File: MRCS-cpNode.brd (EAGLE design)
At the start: 99.8 x 68.8 mm, 46 parts, among them P1 CA CC, U1 MAX3465CPD, U2 NE555P

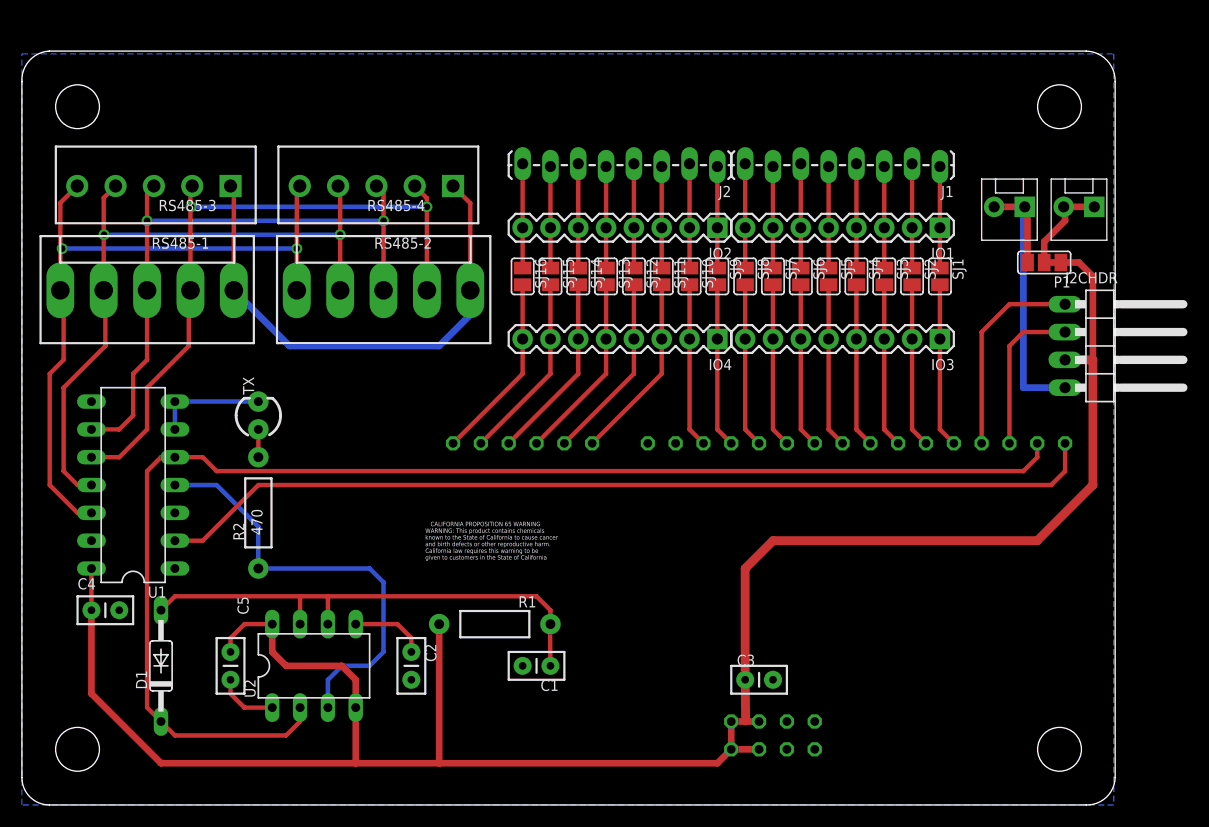
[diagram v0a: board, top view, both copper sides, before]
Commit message: added 6-pin headers, fixed DCR errors
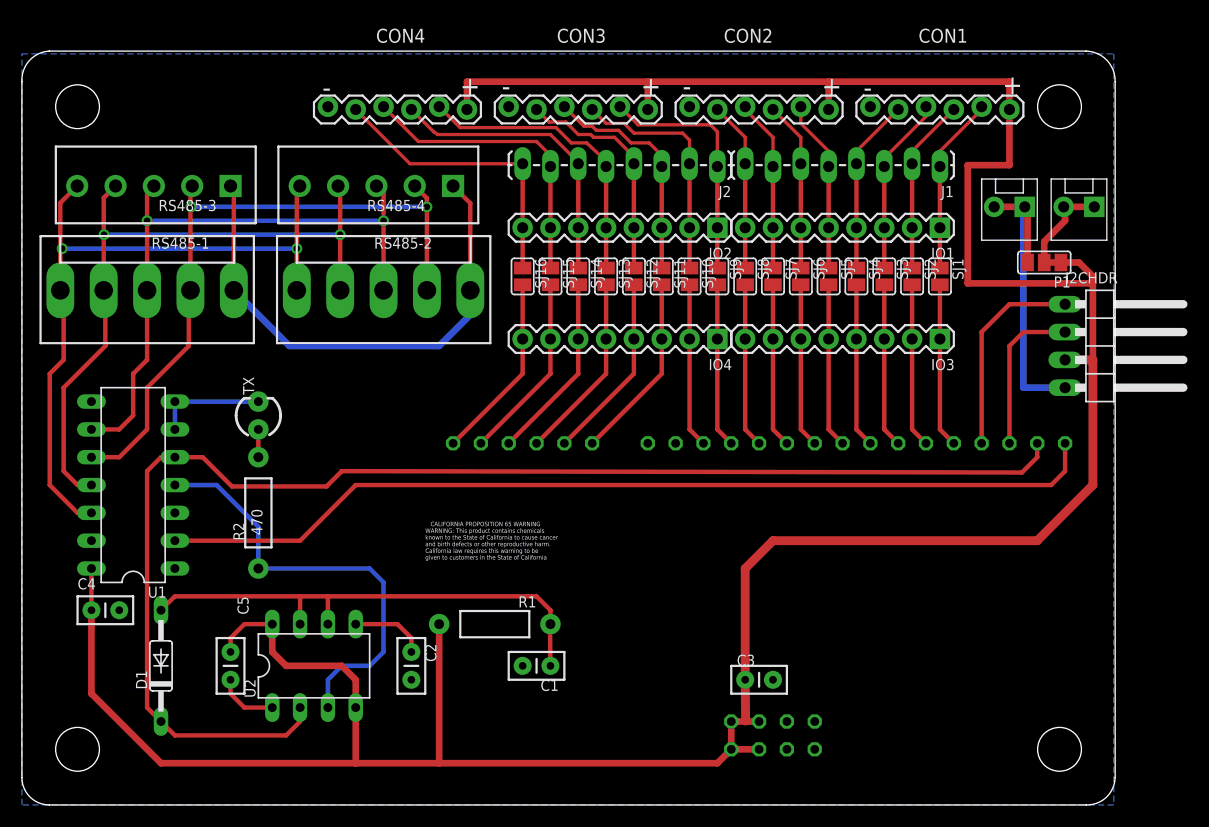
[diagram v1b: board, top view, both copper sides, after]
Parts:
- added CON1, CON2, CON3, CON4: (no value), SPCoast:1X06-SIP_LOCK
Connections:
- removed net N$1: IO1.2, J1.2, SJ2.1
- removed net N$10: IO2.2, J2.2, SJ10.1
- removed net N$2: IO1.1, J1.1, SJ1.1
- removed net N$21: IO2.4, J2.4, SJ12.1
- removed net N$3: IO1.3, J1.3, SJ3.1
- removed net N$30: IO2.5, J2.5, SJ13.1
- removed net N$31: IO2.6, J2.6, SJ14.1
- removed net N$32: IO2.7, J2.7, SJ15.1
- removed net N$33: IO2.8, J2.8, SJ16.1
- removed net N$4: IO1.4, J1.4, SJ4.1
- removed net N$43: IO2.3, J2.3, SJ11.1
- removed net N$5: IO1.5, J1.5, SJ5.1
- removed net N$6: IO1.6, J1.6, SJ6.1
- removed net N$7: IO1.7, J1.7, SJ7.1
- removed net N$8: IO1.8, J1.8, SJ8.1
- removed net N$9: IO2.1, J2.1, SJ9.1
- new net O1: CON1.2, IO1.1, J1.1, SJ1.1
- new net O10: CON3.3, IO2.2, J2.2, SJ10.1
- new net O11: CON3.4, IO2.3, J2.3, SJ11.1
- new net O12: CON3.5, IO2.4, J2.4, SJ12.1
- new net O13: CON4.2, IO2.5, J2.5, SJ13.1
- new net O14: CON4.3, IO2.6, J2.6, SJ14.1
- new net O15: CON4.4, IO2.7, J2.7, SJ15.1
- new net O16: CON4.5, IO2.8, J2.8, SJ16.1
- new net O2: CON1.3, IO1.2, J1.2, SJ2.1
- new net O3: CON1.4, IO1.3, J1.3, SJ3.1
- new net O4: CON1.5, IO1.4, J1.4, SJ4.1
- new net O5: CON2.2, IO1.5, J1.5, SJ5.1
- new net O6: CON2.3, IO1.6, J1.6, SJ6.1
- new net O7: CON2.4, IO1.7, J1.7, SJ7.1
- new net O8: CON2.5, IO1.8, J1.8, SJ8.1
- new net O9: CON3.2, IO2.1, J2.1, SJ9.1
- net GND: now also CON1.6, CON2.6, CON3.6, CON4.6
- net VCC: now also CON1.1, CON2.1, CON3.1, CON4.1
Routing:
- net VCC: track 191.7 -> 282.5 mm
- net O15: track 0.00 -> 27.4 mm
- net O14: track 0.00 -> 27.3 mm
- net O13: track 0.00 -> 27.0 mm
- net O16: track 0.00 -> 26.8 mm
- net O9: track 0.00 -> 22.3 mm
- net O10: track 0.00 -> 21.7 mm
- net O11: track 0.00 -> 21.0 mm
- net O12: track 0.00 -> 20.8 mm
- net O3: track 0.00 -> 16.3 mm
- net O1: track 0.00 -> 16.3 mm
- net O4: track 0.00 -> 16.1 mm
- net O2: track 0.00 -> 16.1 mm
- net O7: track 0.00 -> 15.8 mm
- net O5: track 0.00 -> 15.8 mm
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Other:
- board text added: "+"
- board text added: "-"
- board text added: "2020-01"
- board text added: "v2.6"
- board text removed: "2019-07"
- board text removed: "v2.5Cp"

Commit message: added missing values
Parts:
- BBLEO: value (none) -> Footprint
- CON1, CON2, CON3, CON4, GND, IO1, IO2, IO3, IO4, J1, J2, LEDCOM: value (none) -> 0.100
- R1: value (none) -> 12k
- SJ1, SJ10, SJ11, SJ12, SJ13, SJ14, SJ15, SJ16, SJ2, SJ3, SJ4, SJ5, SJ6, SJ7, SJ8, SJ9: value (none) -> OFF
- TX: value (none) -> G
- U$2: value CA-PROP65WARNING -> Prop65
- U$3: value (none) -> MRCS

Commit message: added missing values
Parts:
- I2CHDR: value (none) -> 0.100
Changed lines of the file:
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@@
 </element>
 <element name="GND" library="SparkFun" package="MOLEX-1X2_LOCK" value="0.100" x="91.44" y="54.61" smashed="yes" rot="R180"/>
-<element name="I2CHDR" library="pinhead" package="1X04/90" value="" x="99.06" y="41.91" smashed="yes" rot="R270">
+<element name="I2CHDR" library="pinhead" package="1X04/90" value="0.100" x="99.06" y="41.91" smashed="yes" rot="R270">
 <attribute name="NAME" x="95.25" y="47.625" size="1.016" layer="25" font="vector" ratio="10"/>
 <attribute name="VALUE" x="94.615" y="34.925" size="1.27" layer="27"/>

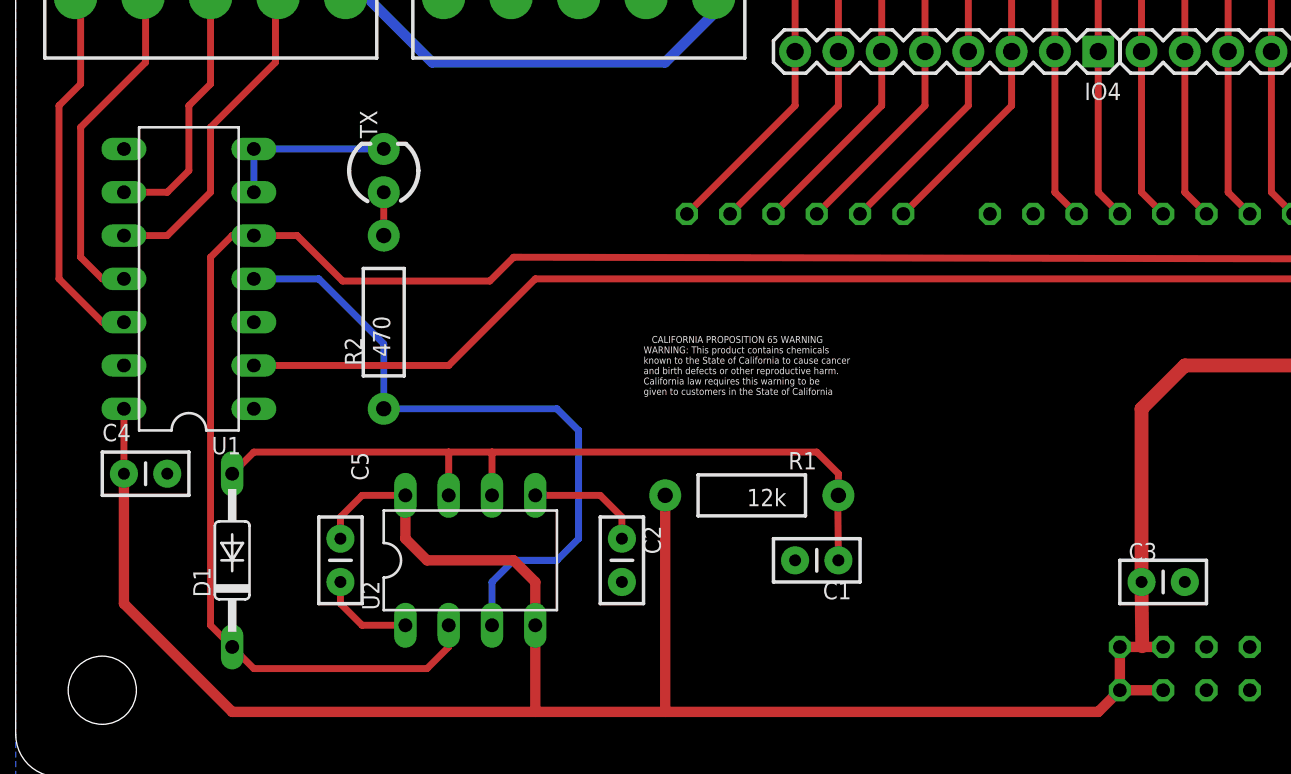
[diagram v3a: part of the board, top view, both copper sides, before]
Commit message: normalized values
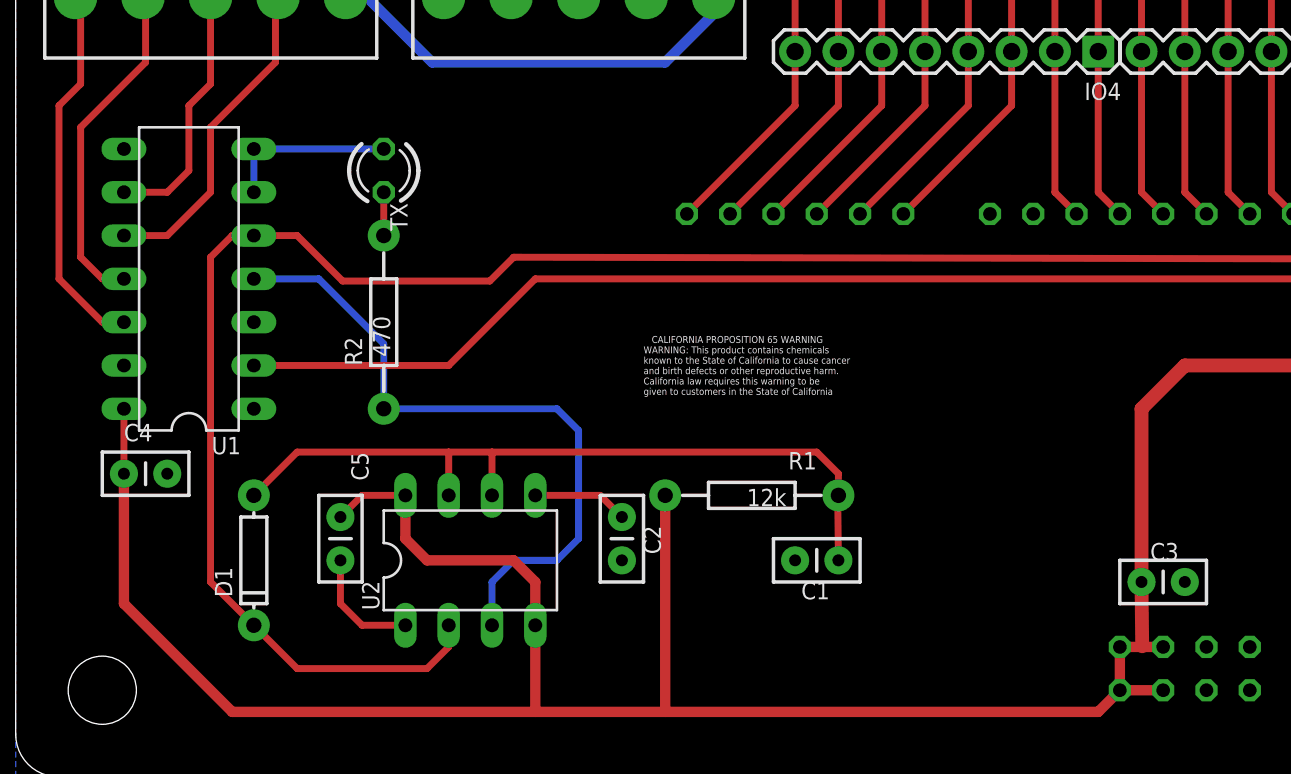
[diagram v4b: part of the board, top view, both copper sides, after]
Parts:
- BOARD1: value BOARD69X100MRCS -> BOARD
- C1: device SparkFun:CAP-PTH-SMALL2 -> SPCoast:C-PTH-0.100
- C2, C3, C4, C5: value .01uF -> 0.01uF; device SparkFun:CAP-PTH-SMALL2 -> SPCoast:C-PTH-0.100
- D1: value 1N4148DO35-10 -> 1N4148; device diode:DO35-10 -> SPCoast:DIODE-1N4148
- R1, R2: device SparkFun:AXIAL-0.4 -> SPCoast:AXIAL-0.4-RES
- RS485-1, RS485-2: value Molex -> 0.156
- TX: device SparkFun-LED:LED3MM -> SPCoast:LED3MM
- moved D1 1.27 mm to (14.0, 12.7)
- moved C4 1.27 mm to (7.62, 17.8)
- moved C1 1.27 mm to (47.0, 12.7)
- moved C3 1.27 mm to (67.3, 11.4)
- turned TX to 270 degrees
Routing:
- net TX: track 123.7 -> 122.3 mm
- net GND: track 44.2 -> 45.4 mm
- net N$38: track 6.88 -> 5.61 mm
- net VCC: track 282.5 -> 281.2 mm
- net N$52: track 46.8 -> 46.0 mm
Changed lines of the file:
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@@
 <elements>
 <element name="BBLEO" library="SPCoast" package="ARDUINO-BBLEO" value="Footprint" x="26.67" y="2.54" smashed="yes"/>
-<element name="BOARD1" library="SPCoast" package="BOARD-DINRAIL-2.71IN-MRCS" value="BOARD69X100MRCS" x="0" y="0" smashed="yes"/>
-<element name="C1" library="SparkFun" package="CAP-PTH-SMALL2" value="0.1uF" x="48.26" y="12.7" smashed="yes" rot="R180">
-<attribute name="NAME" x="49.022" y="11.43" size="1.016" layer="25" font="vector" ratio="10" rot="R180"/>
-<attribute name="VALUE" x="49.911" y="14.859" size="1.016" layer="27" font="vector" ratio="10" rot="R180"/>
-</element>
-<element name="C2" library="SparkFun" package="CAP-PTH-SMALL2" value=".01uF" x="35.56" y="13.97" smashed="yes" rot="R270">
+<element name="BOARD1" library="SPCoast" package="BOARD-DINRAIL-2.71IN-MRCS" value="BOARD" x="0" y="0" smashed="yes"/>
+<element name="C1" library="SPCoast" package="C-PTH-0.100" value="0.1uF" x="46.99" y="12.7" smashed="yes" rot="R180">
+<attribute name="NAME" x="47.752" y="11.43" size="1.016" layer="25" font="vector" ratio="10" rot="R180"/>
+<attribute name="VALUE" x="48.641" y="14.859" size="1.016" layer="27" font="vector" ratio="10" rot="R180"/>
+</element>
+<element name="C2" library="SPCoast" package="C-PTH-0.100" value="0.01uF" x="35.56" y="13.97" smashed="yes" rot="R270">
 <attribute name="NAME" x="36.83" y="14.732" size="1.016" layer="25" font="vector" ratio="10" rot="R270"/>
 <attribute name="VALUE" x="33.401" y="16.256" size="1.016" layer="27" font="vector" ratio="10" rot="R270"/>
 </element>
-<element name="C3" library="SparkFun" package="CAP-PTH-SMALL2" value=".01uF" x="66.04" y="11.43" smashed="yes">
-<attribute name="NAME" x="65.278" y="12.7" size="1.016" layer="25" font="vector" ratio="10"/>
-<attribute name="VALUE" x="64.389" y="9.271" size="1.016" layer="27" font="vector" ratio="10"/>
-</element>
-<element name="C4" library="SparkFun" package="CAP-PTH-SMALL2" value=".01uF" x="6.35" y="17.78" smashed="yes">
-<attribute name="NAME" x="5.08" y="19.685" size="1.016" layer="25" font="vector" ratio="10"/>
-<attribute name="VALUE" x="5.08" y="15.24" size="1.016" layer="27" font="vector" ratio="10"/>
-</element>
-<element name="C5" library="SparkFun" package="CAP-PTH-SMALL2" value=".01uF" x="19.05" y="13.97" smashed="yes" rot="R270">
+<element name="C3" library="SPCoast" package="C-PTH-0.100" value="0.01uF" x="67.31" y="11.43" smashed="yes">
+<attribute name="NAME" x="66.548" y="12.7" size="1.016" layer="25" font="vector" ratio="10"/>
+<attribute name="VALUE" x="65.659" y="9.271" size="1.016" layer="27" font="vector" ratio="10"/>
+</element>
+<element name="C4" library="SPCoast" package="C-PTH-0.100" value="0.01uF" x="7.62" y="17.78" smashed="yes">
+<attribute name="NAME" x="6.35" y="19.685" size="1.016" layer="25" font="vector" ratio="10"/>
+<attribute name="VALUE" x="6.35" y="15.24" size="1.016" layer="27" font="vector" ratio="10"/>
+</element>
+<element name="C5" library="SPCoast" package="C-PTH-0.100" value="0.01uF" x="19.05" y="13.97" smashed="yes" rot="R270">
 <attribute name="NAME" x="19.685" y="19.05" size="1.016" layer="25" font="vector" ratio="10" rot="R270"/>
 <attribute name="VALUE" x="17.78" y="20.32" size="1.016" layer="27" font="vector" ratio="10" rot="R270"/>
@@
 <attribute name="VALUE" x="40.64" y="59.055" size="1.016" layer="27" font="vector" ratio="10" rot="R180"/>
 </element>
-<element name="D1" library="diode" package="DO35-10" value="1N4148DO35-10" x="12.7" y="12.7" smashed="yes" rot="R90">
-<attribute name="NAME" x="11.43" y="10.541" size="1.016" layer="25" font="vector" ratio="10" rot="R90"/>
-<attribute name="VALUE" x="15.367" y="9.271" size="1.016" layer="27" font="vector" ratio="10" rot="R90"/>
+<element name="D1" library="SPCoast" package="DIODE-1N4148" value="1N4148" x="13.97" y="12.7" smashed="yes" rot="R90">
+<attribute name="NAME" x="12.7" y="10.541" size="1.016" layer="25" font="vector" ratio="10" rot="R90"/>
+<attribute name="VALUE" x="16.637" y="9.271" size="1.016" layer="27" font="vector" ratio="10" rot="R90"/>
 </element>
 <element name="GND" library="SparkFun" package="MOLEX-1X2_LOCK" value="0.100" x="91.44" y="54.61" smashed="yes" rot="R180"/>
@@
 <attribute name="VALUE" x="93.4451" y="49.53" size="1.016" layer="27" font="vector" ratio="10" rot="R180"/>
 </element>
-<element name="R1" library="SparkFun" package="AXIAL-0.4" value="12k" x="43.18" y="16.51" smashed="yes" rot="R180">
+<element name="R1" library="SPCoast" package="AXIAL-0.4-RES" value="12k" x="43.18" y="16.51" smashed="yes" rot="R180">
 <attribute name="NAME" x="46.99" y="19.05" size="1.016" layer="25" font="vector" ratio="10" rot="R180"/>
 <attribute name="VALUE" x="45.212" y="16.891" size="1.016" layer="21" font="vector" ratio="15" rot="R180"/>
 </element>
-<element name="R2" library="SparkFun" package="AXIAL-0.4" value="470" x="21.59" y="26.67" smashed="yes" rot="R90">
+<element name="R2" library="SPCoast" package="AXIAL-0.4-RES" value="470" x="21.59" y="26.67" smashed="yes" rot="R90">
 <attribute name="NAME" x="20.32" y="24.13" size="1.016" layer="25" font="vector" ratio="10" rot="R90"/>
 <attribute name="VALUE" x="21.971" y="24.638" size="1.016" layer="21" font="vector" ratio="15" rot="R90"/>
 </element>
-<element name="RS485-1" library="SPCoast" package="KK-156-5" value="Molex" x="11.43" y="46.99" smashed="yes">
+<element name="RS485-1" library="SPCoast" package="KK-156-5" value="0.156" x="11.43" y="46.99" smashed="yes">
 <attribute name="NAME" x="17.145" y="51.81" size="1.016" layer="25" font="vector" ratio="10" rot="R180"/>
 <attribute name="VALUE" x="19.05" y="44.075" size="1.016" layer="27" font="vector" ratio="10" rot="R180"/>
 </element>
-<element name="RS485-2" library="SPCoast" package="KK-156-5" value="Molex" x="33.02" y="46.99" smashed="yes">
+<element name="RS485-2" library="SPCoast" package="KK-156-5" value="0.156" x="33.02" y="46.99" smashed="yes">
 <attribute name="NAME" x="37.465" y="51.81" size="1.016" layer="25" font="vector" ratio="10" rot="R180"/>
 <attribute name="VALUE" x="41.275" y="44.075" size="1.016" layer="27" font="vector" ratio="10" rot="R180"/>
@@
 <attribute name="VALUE" x="63.5" y="47.8599" size="0.02" layer="27" rot="R270"/>
 </element>
-<element name="TX" library="SparkFun-LED" package="LED3MM" value="G" x="21.59" y="35.56" smashed="yes" rot="R90">
-<attribute name="NAME" x="21.209" y="37.465" size="1.016" layer="25" font="vector" ratio="10" rot="R90"/>
-<attribute name="VALUE" x="23.241" y="37.465" size="1.27" layer="27" ratio="10" rot="R90"/>
+<element name="TX" library="SPCoast" package="LED3MM" value="G" x="21.59" y="35.56" smashed="yes" rot="R270">
+<attribute name="NAME" x="21.971" y="33.655" size="1.016" layer="25" font="vector" ratio="10" rot="R270"/>
+<attribute name="VALUE" x="19.939" y="33.655" size="1.27" layer="27" ratio="10" rot="R270"/>
 </element>
 <element name="U$1" library="SparkFun" package="CREATIVE_COMMONS" value="CREATIVE_COMMONS" x="17.78" y="-11.43" smashed="yes"/>
@@
 <wire x1="97.79" y1="40.64" x2="95.25" y2="40.64" width="0.8128" layer="1"/>
 <wire x1="6.35" y1="21.59" x2="6.35" y2="17.78" width="0.4064" layer="1"/>
-<wire x1="19.05" y1="13.97" x2="19.05" y2="15.24" width="0.4064" layer="1"/>
 <wire x1="19.05" y1="15.24" x2="20.32" y2="16.51" width="0.4064" layer="1"/>
 <wire x1="20.32" y1="16.51" x2="22.86" y2="16.51" width="0.4064" layer="1"/>
@@
 <wire x1="13.97" y1="36.83" x2="21.59" y2="36.83" width="0.4064" layer="16"/>
 <wire x1="13.97" y1="36.83" x2="13.97" y2="34.29" width="0.4064" layer="16"/>
-<wire x1="19.05" y1="11.43" x2="19.05" y2="10.16" width="0.4064" layer="1"/>
+<wire x1="19.05" y1="12.7" x2="19.05" y2="10.16" width="0.4064" layer="1"/>
 <wire x1="19.05" y1="10.16" x2="20.32" y2="8.89" width="0.4064" layer="1"/>
 <wire x1="20.32" y1="8.89" x2="22.86" y2="8.89" width="0.4064" layer="1"/>
@@
 <wire x1="30.48" y1="16.51" x2="34.29" y2="16.51" width="0.4064" layer="1"/>
 <wire x1="34.29" y1="16.51" x2="35.56" y2="15.24" width="0.4064" layer="1"/>
-<wire x1="35.56" y1="15.24" x2="35.56" y2="13.97" width="0.4064" layer="1"/>
 </signal>
 <signal name="D3">
@@
 <wire x1="19.177" y1="29.083" x2="16.51" y2="31.75" width="0.4064" layer="1"/>
 <wire x1="16.51" y1="31.75" x2="13.97" y2="31.75" width="0.4064" layer="1"/>
-<wire x1="12.7" y1="7.62" x2="13.97" y2="6.35" width="0.4064" layer="1"/>
-<wire x1="13.97" y1="6.35" x2="24.13" y2="6.35" width="0.4064" layer="1"/>
+<wire x1="13.97" y1="8.89" x2="16.51" y2="6.35" width="0.4064" layer="1"/>
+<wire x1="16.51" y1="6.35" x2="24.13" y2="6.35" width="0.4064" layer="1"/>
 <wire x1="24.13" y1="6.35" x2="25.4" y2="7.62" width="0.4064" layer="1"/>
 <wire x1="25.4" y1="7.62" x2="25.4" y2="8.89" width="0.4064" layer="1"/>
 <wire x1="13.97" y1="31.75" x2="12.7" y2="31.75" width="0.4064" layer="1"/>
 <wire x1="12.7" y1="31.75" x2="11.43" y2="30.48" width="0.4064" layer="1"/>
-<wire x1="11.43" y1="30.48" x2="11.43" y2="8.89" width="0.4064" layer="1"/>
-<wire x1="11.43" y1="8.89" x2="12.7" y2="7.62" width="0.4064" layer="1"/>
+<wire x1="11.43" y1="30.48" x2="11.43" y2="11.43" width="0.4064" layer="1"/>
+<wire x1="11.43" y1="11.43" x2="13.97" y2="8.89" width="0.4064" layer="1"/>
 </signal>
 <signal name="N$52">
@@
 <wire x1="48.26" y1="16.51" x2="48.22" y2="16.47" width="0.4064" layer="1"/>
 <wire x1="48.22" y1="16.47" x2="48.26" y2="12.7" width="0.4064" layer="1"/>
-<wire x1="12.7" y1="17.78" x2="13.97" y2="19.05" width="0.4064" layer="1"/>
-<wire x1="13.97" y1="19.05" x2="25.4" y2="19.05" width="0.4064" layer="1"/>
+<wire x1="13.97" y1="16.51" x2="16.51" y2="19.05" width="0.4064" layer="1"/>
+<wire x1="16.51" y1="19.05" x2="25.4" y2="19.05" width="0.4064" layer="1"/>
 <wire x1="25.4" y1="19.05" x2="27.94" y2="19.05" width="0.4064" layer="1"/>
 <wire x1="27.94" y1="19.05" x2="27.94" y2="16.51" width="0.4064" layer="1"/>
